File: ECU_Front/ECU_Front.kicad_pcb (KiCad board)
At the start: 2 copper layers, 100.5 x 54.9 mm, 19 parts, among them J1 Conn_01x04_Pin, J2 Conn_01x04_Pin, J3 Conn_01x02_Pin, U2 YAAJ_DCDC_StepDown_LM2596, U3 ESP32-DevKitC

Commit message: final fix ECU Front
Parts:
- added C7: 10uF, Capacitor_THT:C_Disc_D5.0mm_W2.5mm_P5.00mm, F.Cu at (156.2, 122.6)
- added C8: 100nF, Capacitor_THT:C_Disc_D5.0mm_W2.5mm_P5.00mm, F.Cu at (152.4, 122.6)
- added G***: LOGO, LOGO, B.Cu at (126.4, 112.4)
- D1: footprint LED_THT:LED_D3.0mm_FlatTop -> LED_THT:LED_D5.0mm
- J1: value Conn_01x04_Pin -> Conn_display; footprint Connector:NS-Tech_Grove_1x04_P2mm_Vertical -> Connector_JST:JST_XH_B4B-XH-A_1x04_P2.50mm_Vertical
- J2: value Conn_01x04_Pin -> Conn_acc; footprint Connector:NS-Tech_Grove_1x04_P2mm_Vertical -> Connector_JST:JST_XH_B4B-XH-A_1x04_P2.50mm_Vertical
- J3: value Conn_01x02_Pin -> Conn_pwr; footprint Connector_PinHeader_2.54mm:PinHeader_1x02_P2.54mm_Vertical -> Connector_JST:JST_XH_B2B-XH-A_1x02_P2.50mm_Vertical
- U2: value YAAJ_DCDC_StepDown_LM2596 -> LM2596_buck
- moved J2 11.2 mm to (162.6, 88.9), turned to 0 degrees
- moved J1 10.6 mm to (186.1, 88.9), turned to 0 degrees
- moved C4 5.35 mm to (196.8, 127.4)
- moved C5 5.06 mm to (180.3, 86.4)
- moved C6 4.97 mm to (175.9, 86.4)
- moved C3 4.57 mm to (200.7, 127.4)
- moved U2 4.22 mm to (136.5, 90.2)
- moved R2 3.89 mm to (145.0, 110.1)
- moved R1 3.89 mm to (145.0, 102.3)
- moved R3 3.89 mm to (177.5, 132.0)
- moved C2 3.61 mm to (142.2, 130.8)
- moved U3 3.51 mm to (160.0, 122.6)
- moved H3 3.37 mm to (208.3, 86.4)
- moved C1 3.29 mm to (148.3, 130.8)
- moved J3 3.29 mm to (145.4, 90.2), turned to -90 degrees
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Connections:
- D1 pad 1: LED_ALIVE -> Net-(D1-K)
- D1 pad 2: Net-(D1-A) -> LED_ALIVE
- J1 pad 2: RXD2 -> TXD2
- J1 pad 3: TXD2 -> RXD2
- J2 pad 2: SDA -> SCL
- J2 pad 3: SCL -> SDA
- R3 pad 1: Net-(D1-A) -> Net-(D1-K)
- U3 pad 1: unconnected-(U3-3V3-Pad1) -> +3V3
- U3 pad 14: unconnected-(U3-GND-Pad14) -> GND
- U3 pad 38: unconnected-(U3-GND-Pad38) -> GND
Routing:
- net +5V: track 196.3 -> 186.8 mm
- net +3V3: track 0.00 -> 7.64 mm
- net Net-(D1-K): track 0.00 -> 6.81 mm
- net Net-(D1-A): track 5.87 -> 0.00 mm
- net SDA: track 8.72 -> 11.5 mm
- net +12V: track 22.3 -> 24.5 mm
- net LED_ALIVE: track 11.4 -> 10.00 mm
- net RXD2: track 8.96 -> 9.54 mm
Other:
- board size 100.5 x 54.9 mm -> 104.8 x 57.8 mm

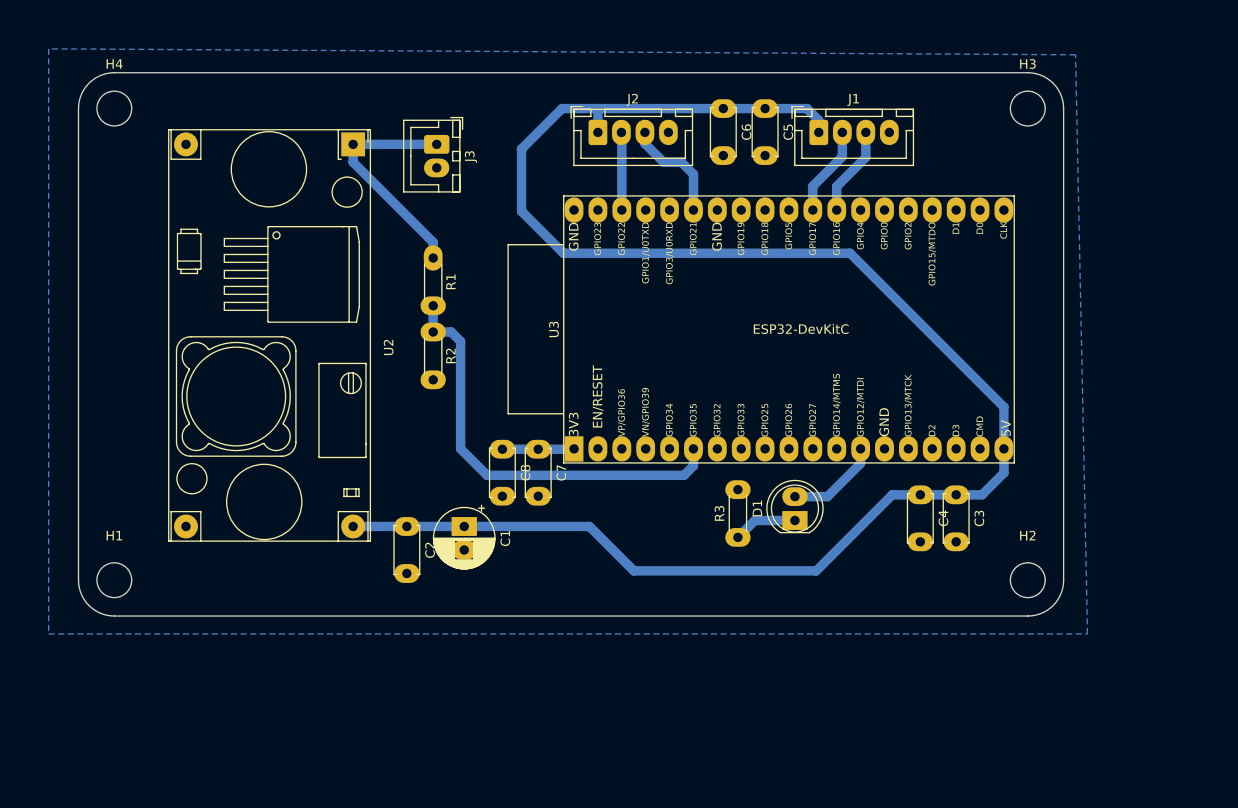
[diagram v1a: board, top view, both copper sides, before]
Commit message: change holes
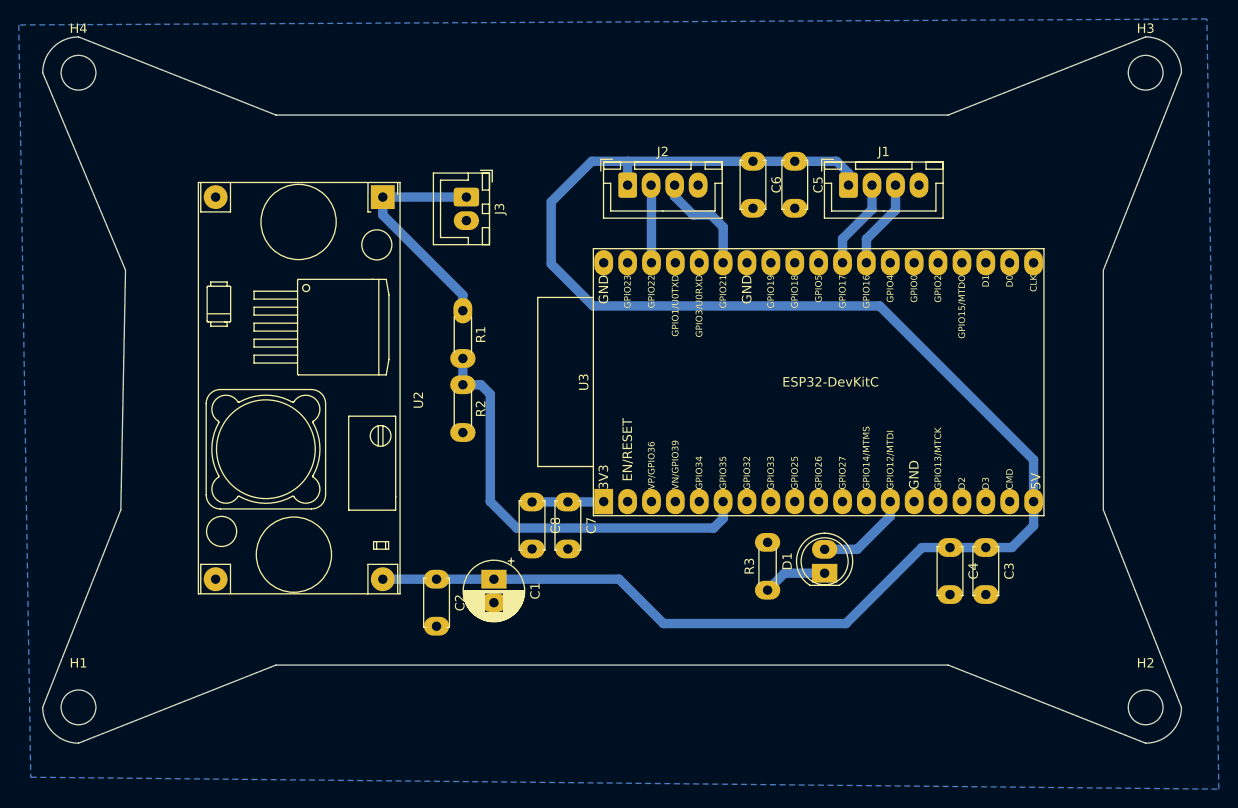
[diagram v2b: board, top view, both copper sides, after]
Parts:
- moved H2 18.4 mm to (220.8, 150.1)
- moved H1 14.1 mm to (107.3, 150.1)
- moved H3 13.1 mm to (220.8, 82.5)
- moved C3 6.43 mm to (203.8, 133.1)
- moved C4 6.43 mm to (200.0, 133.1)
- moved G*** 6.43 mm to (129.5, 118.0)
- moved C1 6.43 mm to (151.5, 136.4)
- moved C2 6.43 mm to (145.4, 136.4)
- moved C5 6.43 mm to (183.5, 92.0)
- moved C6 6.43 mm to (179.1, 92.0)
- moved C7 6.43 mm to (159.4, 128.2)
- moved C8 6.43 mm to (155.6, 128.2)
- moved J3 6.43 mm to (148.6, 95.8)
- moved R1 6.43 mm to (148.2, 107.9)
- moved R2 6.43 mm to (148.2, 115.7)
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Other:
- board size 104.8 x 57.8 mm -> 121.1 x 75.1 mm
